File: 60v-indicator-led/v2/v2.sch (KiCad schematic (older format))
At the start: 12 parts, among them J1 HV-IN

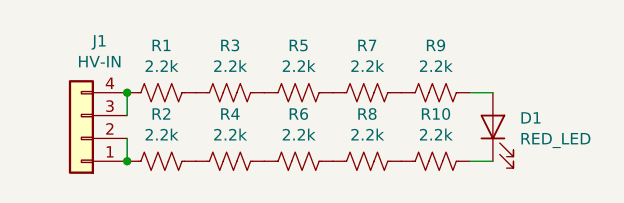
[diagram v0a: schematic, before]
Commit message: Made lots of gerbers, shipped boards.
Also, re-routed interface-board to be 8/8mil minimum spacing.
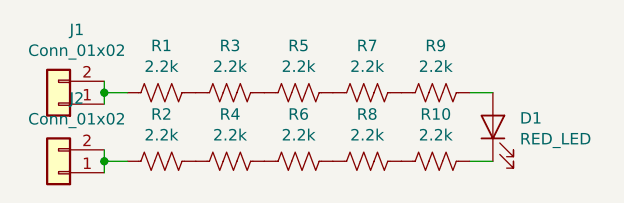
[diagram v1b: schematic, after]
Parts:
- removed J1: HV-IN, Connector_TE-Connectivity:TE_MATE-N-LOK_1-770870-x_1x03_P4.14mm_Vertical, symbol Connector_Generic:Conn_01x04
- added J1, J2: Conn_01x02, Connector_TE-Connectivity:TE_MATE-N-LOK_1-770866-x_1x02_P4.14mm_Vertical, symbol Connector_Generic:Conn_01x02
- D1: footprint LED_THT:LED_D5.0mm -> CustomFootprints:LPA-C011301S-x LED 0805 LIGHT PIPE SINGLE VERT SMD
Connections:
- net at R2.2: now also J2.1 (Pin_1), J2.2 (Pin_2)
- net at R1.2: now also J1.1 (Pin_1), J1.2 (Pin_2)
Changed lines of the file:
@@
 EESchema Schematic File Version 4
+LIBS:v2-cache
 EELAYER 26 0
 EELAYER END
@@
 Comment4 ""
 $EndDescr
-$Comp
-L Connector_Generic:Conn_01x04 J1
-U 1 1 5C6F2EFC
-P 1850 3500
-F 0 "J1" H 1770 3075 50  0000 C CNN
-F 1 "HV-IN" H 1770 3166 50  0000 C CNN
-F 2 "Connector_TE-Connectivity:TE_MATE-N-LOK_1-770870-x_1x03_P4.14mm_Vertical" H 1850 3500 50  0001 C CNN
-F 3 "~" H 1850 3500 50  0001 C CNN
-	1    1850 3500
-	-1   0    0    1
-$EndComp
 $Comp
 L Device:R_US R1
@@
 	0    1    1    0
 $EndComp
-Wire Wire Line
-	2050 3400 2050 3300
-Connection ~ 2050 3300
-Wire Wire Line
-	2050 3500 2050 3600
-Connection ~ 2050 3600
 $Comp
 L Device:LED D1
@@
 F 0 "D1" V 3688 3332 50  0000 R CNN
 F 1 "RED_LED" V 3597 3332 50  0000 R CNN
-F 2 "LED_THT:LED_D5.0mm" H 3650 3450 50  0001 C CNN
+F 2 "CustomFootprints:LPA-C011301S-x LED 0805 LIGHT PIPE SINGLE VERT SMD" H 3650 3450 50  0001 C CNN
 F 3 "~" H 3650 3450 50  0001 C CNN
 	1    3650 3450
@@
 Wire Wire Line
 	3650 3600 3550 3600
+$Comp
+L Connector_Generic:Conn_01x02 J1
+U 1 1 5C809112
+P 1750 3350
+F 0 "J1" H 1670 3025 50  0000 C CNN
+F 1 "Conn_01x02" H 1670 3116 50  0000 C CNN
+F 2 "Connector_TE-Connectivity:TE_MATE-N-LOK_1-770866-x_1x02_P4.14mm_Vertical" H 1750 3350 50  0001 C CNN
+F 3 "~" H 1750 3350 50  0001 C CNN
+	1    1750 3350
+	-1   0    0    1
+$EndComp
+$Comp
+L Connector_Generic:Conn_01x02 J2
+U 1 1 5C80917C
+P 1750 3650
+F 0 "J2" H 1670 3325 50  0000 C CNN
+F 1 "Conn_01x02" H 1670 3416 50  0000 C CNN
+F 2 "Connector_TE-Connectivity:TE_MATE-N-LOK_1-770866-x_1x02_P4.14mm_Vertical" H 1750 3650 50  0001 C CNN
+F 3 "~" H 1750 3650 50  0001 C CNN
+	1    1750 3650
+	-1   0    0    1
+$EndComp
+Wire Wire Line
+	2050 3300 1950 3300
+Wire Wire Line
+	1950 3300 1950 3250
+Wire Wire Line
+	1950 3350 1950 3300
+Connection ~ 1950 3300
+Wire Wire Line
+	2050 3600 1950 3600
+Wire Wire Line
+	1950 3600 1950 3550
+Wire Wire Line
+	1950 3650 1950 3600
+Connection ~ 1950 3600
 $EndSCHEMATC

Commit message: Made BOM etc for 60v-indicator-led
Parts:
- R1, R10, R2, R3, R4, R5, R6, R7, R8, R9: value 2.2k -> 1k
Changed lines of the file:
@@
 P 2200 3300
 F 0 "R1" V 1995 3300 50  0000 C CNN
-F 1 "2.2k" V 2086 3300 50  0000 C CNN
+F 1 "1k" V 2086 3300 50  0000 C CNN
 F 2 "Resistor_SMD:R_0805_2012Metric" V 2240 3290 50  0001 C CNN
 F 3 "~" H 2200 3300 50  0001 C CNN
@@
 P 2500 3300
 F 0 "R3" V 2295 3300 50  0000 C CNN
-F 1 "2.2k" V 2386 3300 50  0000 C CNN
+F 1 "1k" V 2386 3300 50  0000 C CNN
 F 2 "Resistor_SMD:R_0805_2012Metric" V 2540 3290 50  0001 C CNN
 F 3 "~" H 2500 3300 50  0001 C CNN
@@
 P 2800 3300
 F 0 "R5" V 2595 3300 50  0000 C CNN
-F 1 "2.2k" V 2686 3300 50  0000 C CNN
+F 1 "1k" V 2686 3300 50  0000 C CNN
 F 2 "Resistor_SMD:R_0805_2012Metric" V 2840 3290 50  0001 C CNN
 F 3 "~" H 2800 3300 50  0001 C CNN
@@
 P 3100 3300
 F 0 "R7" V 2895 3300 50  0000 C CNN
-F 1 "2.2k" V 2986 3300 50  0000 C CNN
+F 1 "1k" V 2986 3300 50  0000 C CNN
 F 2 "Resistor_SMD:R_0805_2012Metric" V 3140 3290 50  0001 C CNN
 F 3 "~" H 3100 3300 50  0001 C CNN
@@
 P 3400 3300
 F 0 "R9" V 3195 3300 50  0000 C CNN
-F 1 "2.2k" V 3286 3300 50  0000 C CNN
+F 1 "1k" V 3286 3300 50  0000 C CNN
 F 2 "Resistor_SMD:R_0805_2012Metric" V 3440 3290 50  0001 C CNN
 F 3 "~" H 3400 3300 50  0001 C CNN
@@
 P 2200 3600
 F 0 "R2" V 1995 3600 50  0000 C CNN
-F 1 "2.2k" V 2086 3600 50  0000 C CNN
+F 1 "1k" V 2086 3600 50  0000 C CNN
 F 2 "Resistor_SMD:R_0805_2012Metric" V 2240 3590 50  0001 C CNN
 F 3 "~" H 2200 3600 50  0001 C CNN
@@
 P 2500 3600
 F 0 "R4" V 2295 3600 50  0000 C CNN
-F 1 "2.2k" V 2386 3600 50  0000 C CNN
+F 1 "1k" V 2386 3600 50  0000 C CNN
 F 2 "Resistor_SMD:R_0805_2012Metric" V 2540 3590 50  0001 C CNN
 F 3 "~" H 2500 3600 50  0001 C CNN
@@
 P 2800 3600
 F 0 "R6" V 2595 3600 50  0000 C CNN
-F 1 "2.2k" V 2686 3600 50  0000 C CNN
+F 1 "1k" V 2686 3600 50  0000 C CNN
 F 2 "Resistor_SMD:R_0805_2012Metric" V 2840 3590 50  0001 C CNN
 F 3 "~" H 2800 3600 50  0001 C CNN
@@
 P 3100 3600
 F 0 "R8" V 2895 3600 50  0000 C CNN
-F 1 "2.2k" V 2986 3600 50  0000 C CNN
+F 1 "1k" V 2986 3600 50  0000 C CNN
 F 2 "Resistor_SMD:R_0805_2012Metric" V 3140 3590 50  0001 C CNN
 F 3 "~" H 3100 3600 50  0001 C CNN
@@
 P 3400 3600
 F 0 "R10" V 3195 3600 50  0000 C CNN
-F 1 "2.2k" V 3286 3600 50  0000 C CNN
+F 1 "1k" V 3286 3600 50  0000 C CNN
 F 2 "Resistor_SMD:R_0805_2012Metric" V 3440 3590 50  0001 C CNN
 F 3 "~" H 3400 3600 50  0001 C CNN
